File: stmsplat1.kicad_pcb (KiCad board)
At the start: 2 copper layers, 63 parts, among them CN1 Conn_01x16_Male, CN2 Conn_01x30_Male, CN3 Conn_01x20_Male, CN4 Conn_01x34_Male, CN5 10n, J1 Conn_Coaxial, J2 Conn_01x04_Male, U1 NUCLEO144-F746ZG, U10 MPL315A2, U11 XBee_SMT, U2 ublox_chinese_PCB_module, U3 HMC544A-RF_Switch, U4 Opamp_Quad_MCP6024, U5 AD8310, U6 MCP6S93-X_UN, U7 ADG729, U8 74HC04, U9 HMC544A-RF_Switch

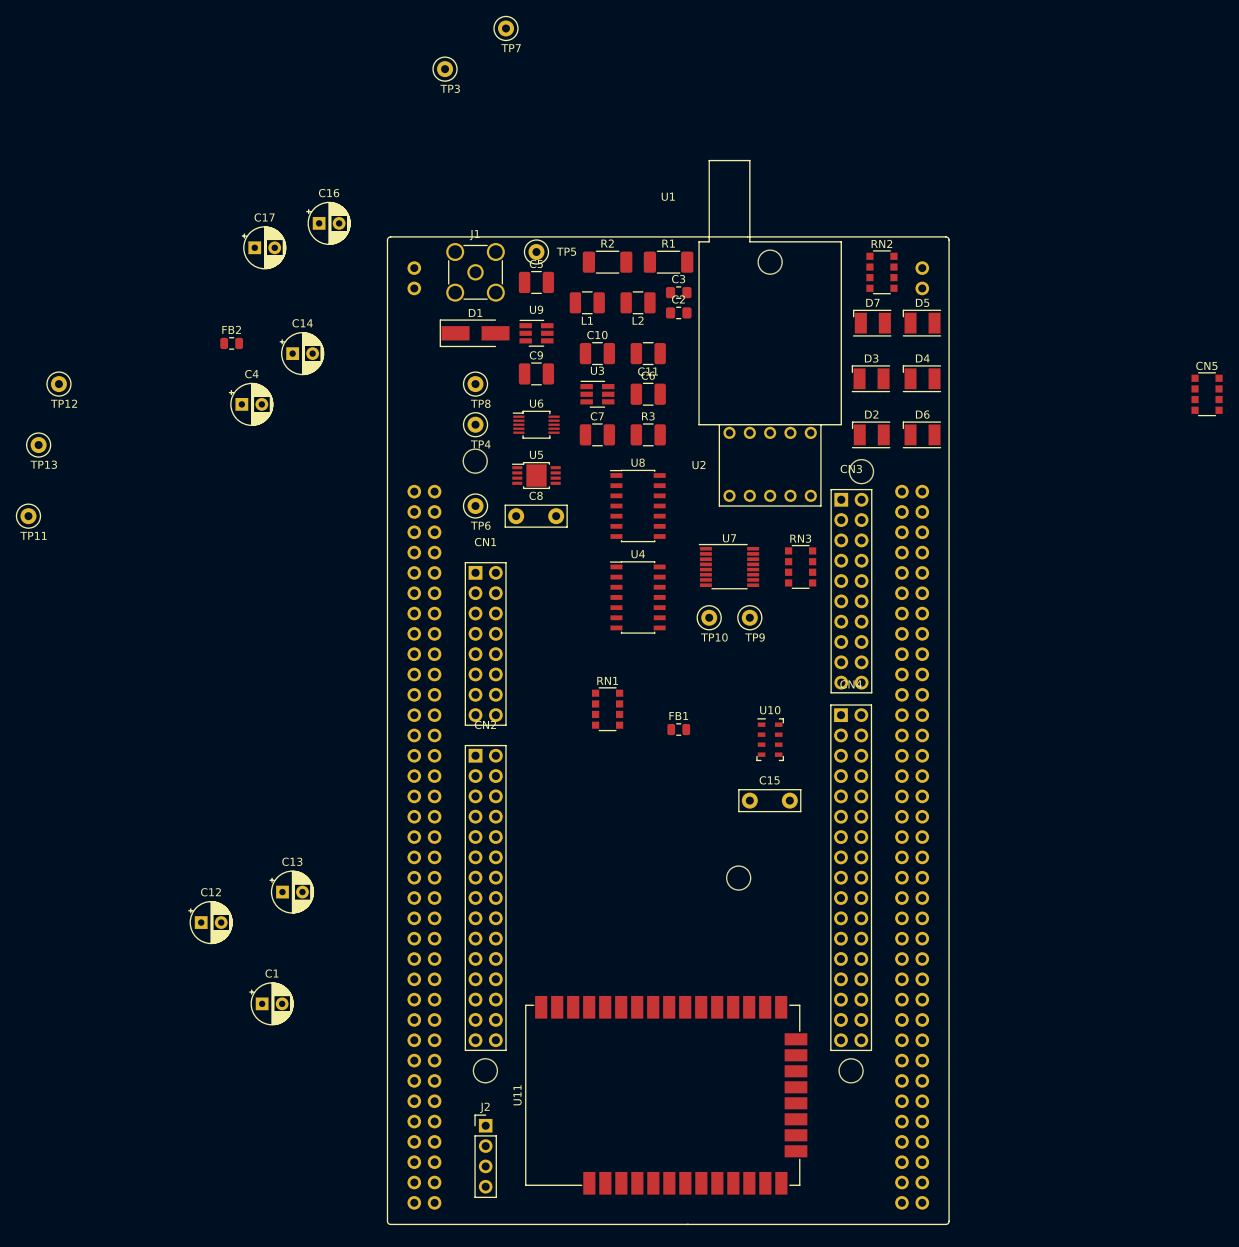
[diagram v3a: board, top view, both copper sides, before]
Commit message: XBee changes, more STM interconnect detail
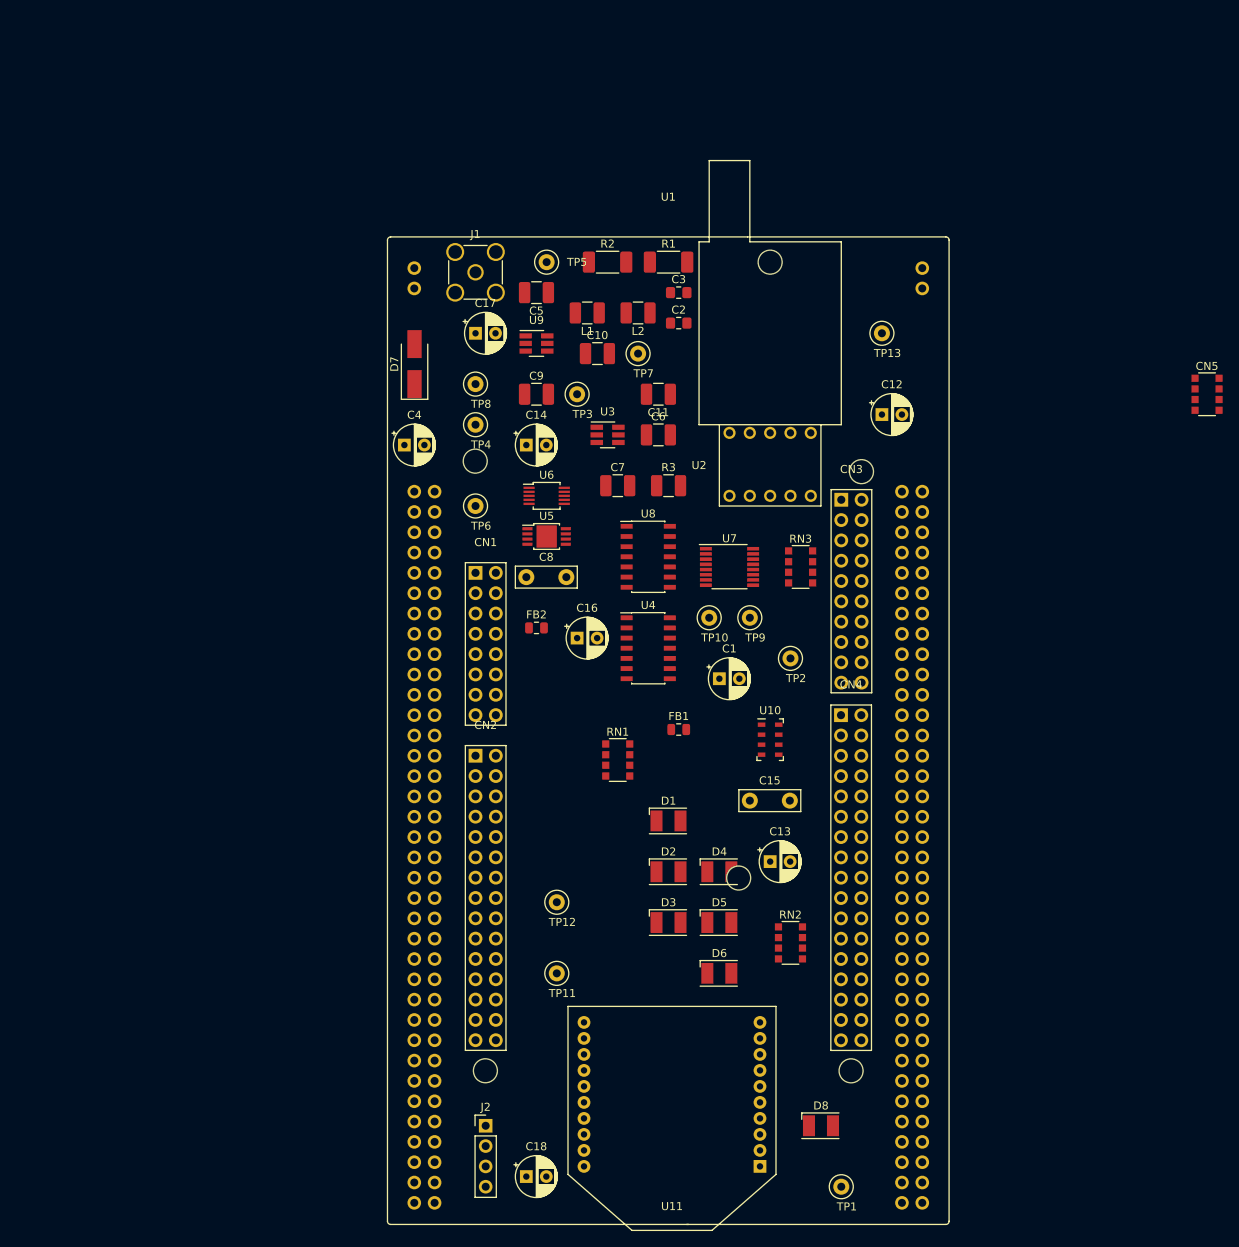
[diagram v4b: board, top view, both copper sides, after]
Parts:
- added C18: 10uF, Capacitor_THT:CP_Radial_D5.0mm_P2.50mm, F.Cu at (72.4, 151.1)
- added D8: LED, LED_SMD:LED_PLCC-2, F.Cu at (109.2, 144.8)
- added TP1: TestPoint, TestPoint:TestPoint_Loop_D1.80mm_Drill1.0mm_Beaded, F.Cu at (111.8, 152.4)
- added TP2: TestPoint, TestPoint:TestPoint_Loop_D1.80mm_Drill1.0mm_Beaded, F.Cu at (105.4, 86.4)
- D1: value SMAJ8.0CA Bourns 9V -> LED; footprint Diode_SMD:D_SMA_Handsoldering -> LED_SMD:LED_PLCC-2
- D7: value LED -> SMAJ8.0CA Bourns 9V; footprint LED_SMD:LED_PLCC-2 -> Diode_SMD:D_SMA_Handsoldering
- U11: value XBee_SMT -> XBee3; footprint RF_Module:Digi_XBee_SMT -> spatboard:XBEE-22MM-TH
- moved TP13 106.3 mm to (116.8, 45.7)
- moved C12 106.2 mm to (116.8, 55.9)
- moved TP12 89.8 mm to (76.2, 116.8)
- moved TP11 87.3 mm to (76.2, 125.7)
- moved RN2 84.6 mm to (105.4, 121.9)
- moved D5 79.1 mm to (96.5, 119.4)
- moved D3 72.6 mm to (90.2, 119.4)
- moved D6 71.9 mm to (96.5, 125.7)
- moved C1 70.1 mm to (96.5, 88.9)
- moved D4 66.7 mm to (96.5, 113.0)
- moved D1 65.6 mm to (90.2, 106.7)
- moved C13 61.1 mm to (102.9, 111.8)
- moved C16 61.0 mm to (78.7, 83.8)
- moved D2 60.2 mm to (90.2, 113.0)
- moved D7 57.5 mm to (58.4, 49.6), turned to 90 degrees
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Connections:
- D1 pad 1: Net-(C5-Pad1) -> GND
- D1 pad 2: AGND -> Net-(D1-Pad2)
- D7 pad 1: GND -> Net-(C5-Pad1)
- D7 pad 2: Net-(D7-Pad2) -> AGND
- FB2 pad 2: Net-(FB2-Pad2) -> GND
- J2 pad 2: /NXRX -> /PC12
- J2 pad 3: /NXTX -> /PB12
- RN2 pad 1: Net-(D4-Pad2) -> Net-(D1-Pad2)
- RN2 pad 2: Net-(D3-Pad2) -> Net-(D2-Pad2)
- RN2 pad 3: Net-(D2-Pad2) -> Net-(D4-Pad2)
- RN2 pad 4: Net-(D5-Pad2) -> Net-(D3-Pad2)
- RN2 pad 5: Net-(RN2-Pad5) -> /PD14
- RN2 pad 6: Net-(RN2-Pad6) -> /PD13
- RN2 pad 7: Net-(RN2-Pad7) -> /PD12
- RN2 pad 8: Net-(RN2-Pad8) -> /PD11
- RN3 pad 1: Net-(D7-Pad2) -> Net-(D5-Pad2)
- RN3 pad 2: Net-(RN3-Pad2) -> GND
- RN3 pad 7: Net-(RN3-Pad7) -> /XB_PIO4
- RN3 pad 8: Net-(RN3-Pad8) -> /PD15
- TP13 pad 1: Net-(TP13-Pad1) -> GND
- U11 pad 1: Net-(U11-Pad1) -> /+3V3
- U11 pad 10: Net-(U11-Pad10) -> GND
- U11 pad 12: Net-(U11-Pad12) -> /PA15
- U11 pad 16: Net-(U11-Pad16) -> /PB15
- U11 pad 19: Net-(U11-Pad19) -> Net-(TP12-Pad1)
- U11 pad 2: Net-(U11-Pad2) -> /PC11
- U11 pad 20: Net-(U11-Pad20) -> Net-(TP11-Pad1)
- U11 pad 3: Net-(U11-Pad3) -> /PA0
- U8 pad 1: Net-(U8-Pad1) -> /PE14

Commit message: Initial design captured
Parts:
- removed CN5: 10n, spatboard:C_Array_Convex_4x1206
- added C19: 1uF, Capacitor_THT:CP_Radial_D5.0mm_P2.50mm, F.Cu at (76.2, 95.2)
- added C20: 470pF, Capacitor_SMD:C_0805_2012Metric_Pad1.15x1.40mm_HandSolder, F.Cu at (74.3, 91.4)
- added LS1: Speaker, Buzzer_Beeper:MagneticBuzzer_Kingstate_KCG0601, F.Cu at (78.7, 109.2)
- added RN4: 4K7, Resistor_SMD:R_Array_Convex_4x1206, F.Cu at (119.4, 58.4)
- added U12: MIC5219-3.3YM5, Package_TO_SOT_SMD:SOT-23-5, F.Cu at (74.3, 88.2)
- moved TP7 41.3 mm to (78.7, 88.9)
- moved C12 5.68 mm to (119.4, 50.8)
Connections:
- net Net-(U7-Pad11) renamed /SPEAKER_TIM4CH3
- C1 pad 1: /+3V3 -> /P3V3
- C12 pad 1: /+3V3 -> /P3V3
- C13 pad 1: /+3V3 -> /P3V3
- C16 pad 1: /+3V3 -> /P3V3
- C18 pad 1: /+3V3 -> /P3V3
- FB1 pad 1: /+3V3 -> /P3V3
- RN2 pad 5: /PD14 -> /PD13
- RN2 pad 6: /PD13 -> /PD14
- RN3 pad 5: /+3V3 -> /P3V3
- TP3 pad 1: Net-(C9-Pad2) -> Net-(TP3-Pad1)
- TP7 pad 1: Net-(C10-Pad2) -> Net-(TP7-Pad1)
- TP9 pad 1: /DAC1 -> Net-(TP9-Pad1)
- U10 pad 1: /+3V3 -> /P3V3
- U10 pad 4: /+3V3 -> /P3V3
- U11 pad 1: /+3V3 -> /P3V3
- U11 pad 5: Net-(D8-Pad2) -> /PE15
- U11 pad 9: Net-(U11-Pad9) -> /PE10
- U2 pad 1: /+3V3 -> /P3V3
- U2 pad 5: Net-(U2-Pad5) -> /PB10
- U4 pad 1: Net-(U4-Pad1) -> Net-(TP3-Pad1)
- U4 pad 13: Net-(U4-Pad13) -> Net-(C19-Pad1)
- U4 pad 14: Net-(U4-Pad14) -> Net-(C19-Pad1)
- U4 pad 2: Net-(U4-Pad2) -> Net-(TP3-Pad1)
- U4 pad 3: Net-(U4-Pad3) -> /PA3
- U4 pad 5: Net-(U4-Pad5) -> Net-(U4-Pad12)
- U4 pad 6: Net-(U4-Pad6) -> Net-(TP9-Pad1)
- U4 pad 7: Net-(U4-Pad7) -> Net-(TP9-Pad1)
- U6 pad 6: Net-(U6-Pad6) -> /PG2
- U6 pad 7: Net-(U6-Pad7) -> /PC3
- U6 pad 8: Net-(U6-Pad8) -> /PC2
- U6 pad 9: Net-(U6-Pad9) -> /PD3
- U7 pad 10: Net-(U7-Pad10) -> /DAC1
- U7 pad 12: Net-(U7-Pad12) -> /LOGOUT
- U7 pad 8: Net-(U7-Pad8) -> /PA3
- U7 pad 9: Net-(U7-Pad9) -> Net-(U4-Pad12)
- U8 pad 14: /+3V3 -> /P3V3
- U8 pad 8: Net-(U8-Pad8) -> Net-(TP7-Pad1)
- U8 pad 9: Net-(U8-Pad9) -> Net-(U11-Pad7)

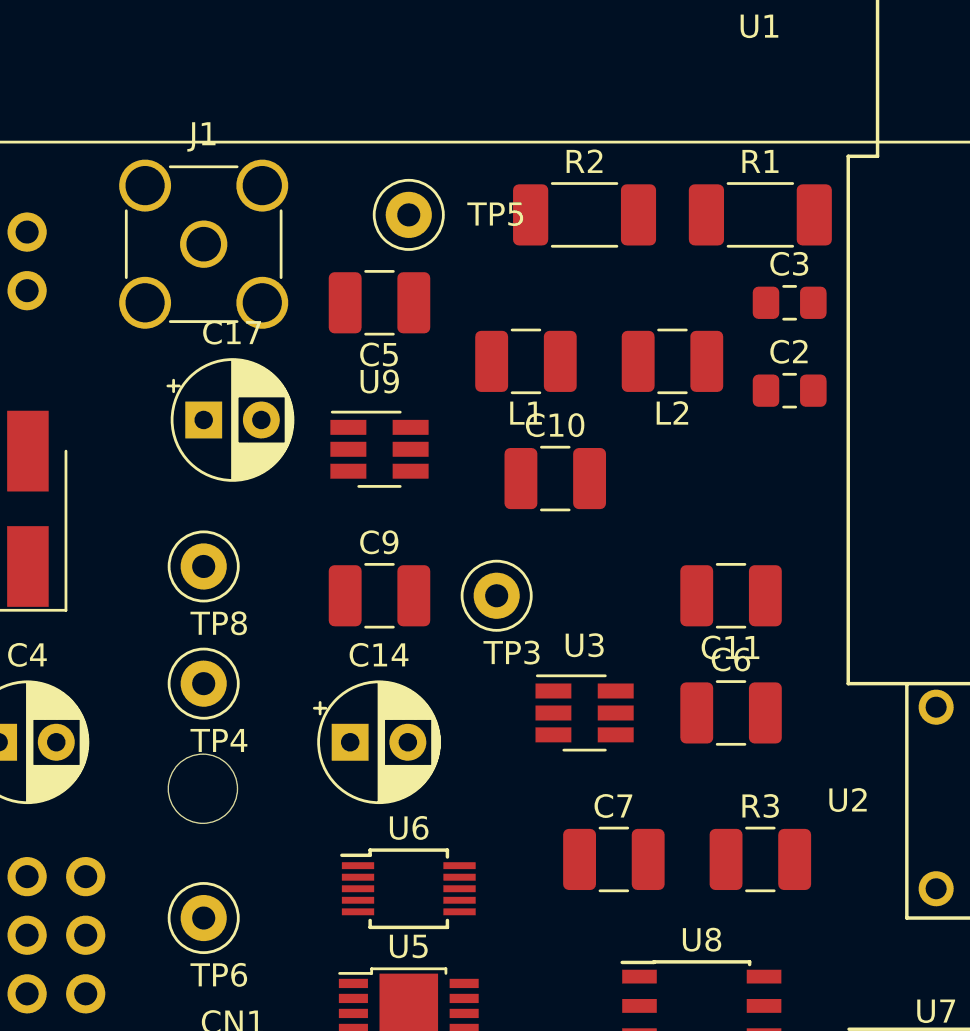
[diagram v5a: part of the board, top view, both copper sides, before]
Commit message: Chenged input and filter matching arrangement
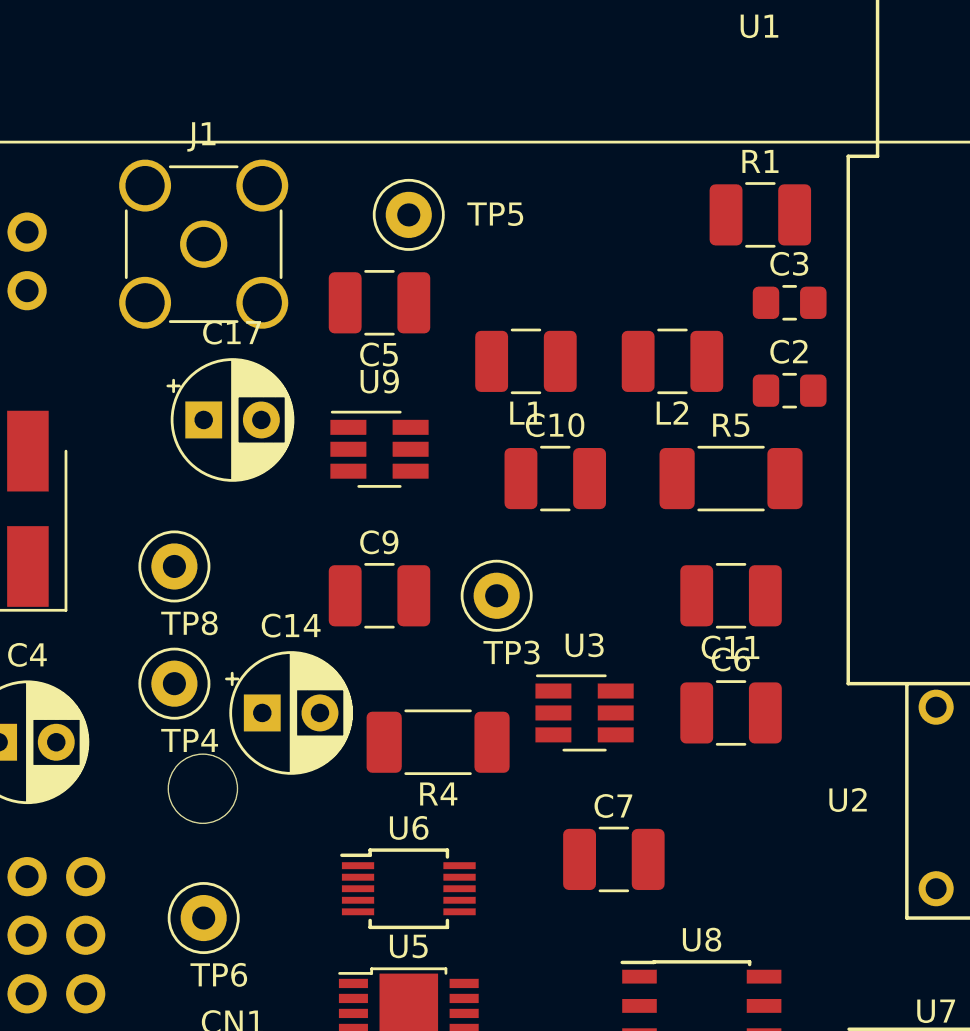
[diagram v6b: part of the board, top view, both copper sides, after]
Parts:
- removed R2: 100R, Resistor_SMD:R_2010_5025Metric_Pad1.52x2.65mm_HandSolder
- removed R3: 53R, Capacitor_SMD:C_1210_3225Metric_Pad1.42x2.65mm_HandSolder
- added R4: 100R, Resistor_SMD:R_2010_5025Metric_Pad1.52x2.65mm_HandSolder, F.Cu at (76.2, 59.7)
- added R5: 100R, Resistor_SMD:R_2010_5025Metric_Pad1.52x2.65mm_HandSolder, F.Cu at (88.9, 48.3)
- R1: value 100R -> 53R; footprint Resistor_SMD:R_2010_5025Metric_Pad1.52x2.65mm_HandSolder -> Capacitor_SMD:C_1210_3225Metric_Pad1.42x2.65mm_HandSolder
- moved C14 4.02 mm to (68.6, 58.4)
- moved TP4 1.27 mm to (64.8, 57.1)
- moved TP8 1.27 mm to (64.8, 52.1)
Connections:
- R1 pad 1: Net-(C10-Pad2) -> Net-(C5-Pad2)
- RN1 pad 2: Net-(C11-Pad1) -> Net-(RN1-Pad2)
- U11 pad 5: /PE15 -> Net-(D8-Pad2)

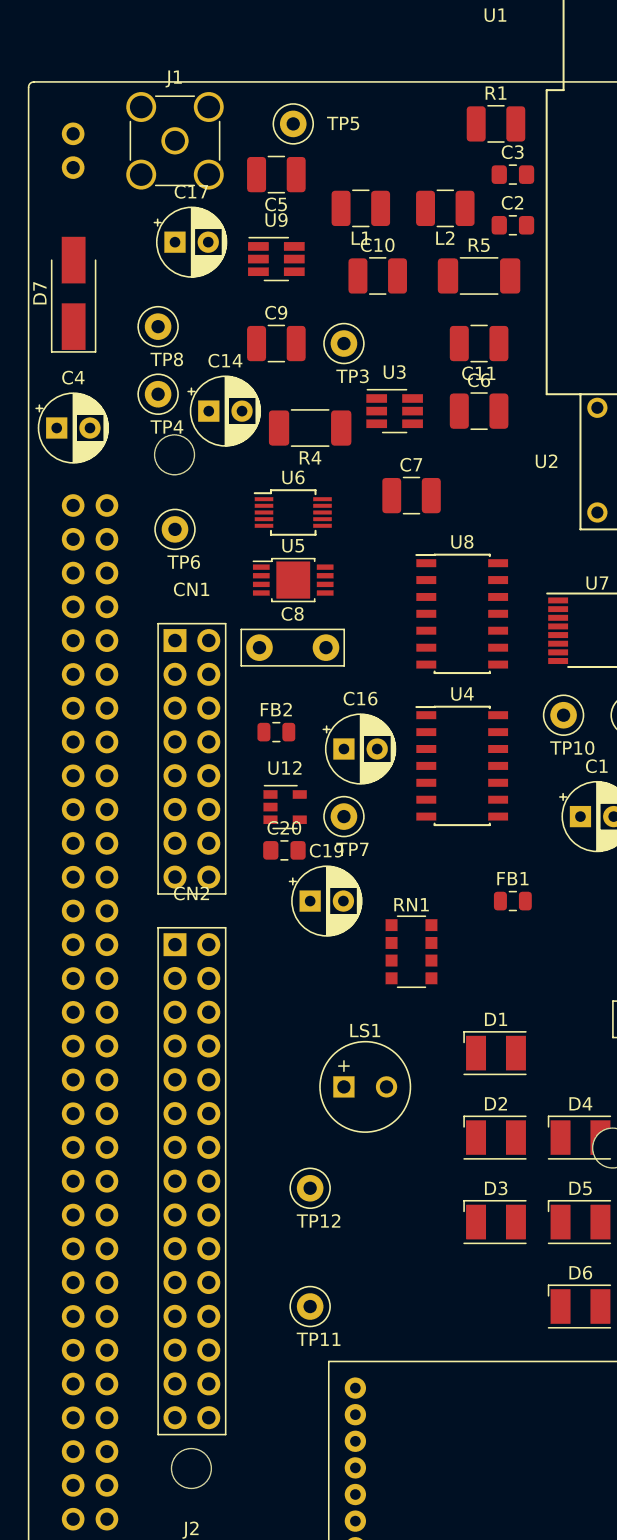
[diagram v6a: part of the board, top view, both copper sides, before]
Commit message: Add GPS and Debug Serial Comms connections
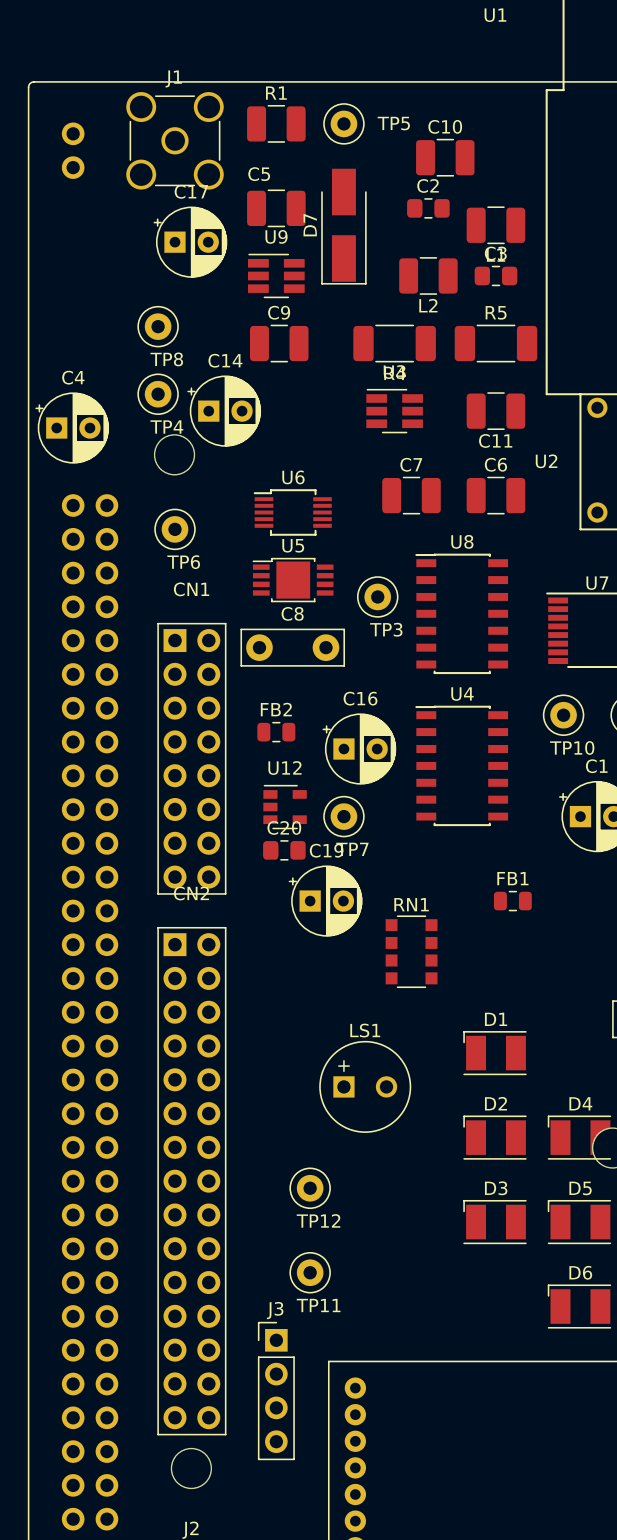
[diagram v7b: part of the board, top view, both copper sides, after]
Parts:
- added J3: Conn_01x04_Male, Connector_PinHeader_2.54mm:PinHeader_1x04_P2.54mm_Vertical, F.Cu at (73.7, 128.3)
- moved D7 21.0 mm to (78.7, 44.5)
- moved TP3 19.2 mm to (81.3, 72.4)
- moved R1 16.5 mm to (73.7, 36.8)
- moved C10 10.2 mm to (86.4, 39.4)
- moved L1 10.2 mm to (90.2, 44.5)
- moved R4 8.98 mm to (82.5, 53.3)
- moved C3 7.73 mm to (90.2, 48.3)
- moved C2 6.48 mm to (85.1, 43.2)
- moved C6 6.48 mm to (90.2, 64.8)
- moved R5 5.24 mm to (90.2, 53.3)
- moved C11 5.24 mm to (90.2, 58.4)
- moved L2 5.24 mm to (85.1, 48.3)
- moved TP5 3.81 mm to (78.7, 36.8)
- moved TP11 2.54 mm to (76.2, 123.2)
- moved C5 2.54 mm to (73.7, 43.2)
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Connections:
- U11 pad 5: Net-(D8-Pad2) -> /PE15
- U2 pad 3: Net-(U2-Pad3) -> /PG9
- U2 pad 4: Net-(U2-Pad4) -> /PC6

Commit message: placement improvements
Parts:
- U5: footprint Package_SO:MSOP-8-1EP_3x3mm_P0.65mm_EP2.54x2.8mm -> Package_SO:MSOP-8_3x3mm_P0.65mm
- moved TP2 57.1 mm to (59.7, 52.1)
- moved RN3 36.9 mm to (105.4, 111.8)
- moved C18 36.6 mm to (106.7, 138.4)
- moved C4 32.6 mm to (87.6, 71.1)
- moved FB1 26.9 mm to (82.5, 69.8)
- moved TP7 25.3 mm to (102.9, 81.3)
- moved C13 23.0 mm to (105.4, 88.9)
- moved TP10 20.4 mm to (96.5, 101.6)
- moved RN1 19.8 mm to (97.8, 85.1)
- moved U7 19.1 mm to (96.5, 94.0)
- moved C1 17.0 mm to (104.1, 73.7)
- moved C15 15.7 mm to (85.1, 100.3)
- moved U10 15.5 mm to (87.6, 94.0)
- moved D4 14.2 mm to (90.2, 125.7)
- moved TP4 8.98 mm to (66.0, 66.0)
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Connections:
- U8 pad 11: Net-(RN4-Pad2) -> Net-(RN4-Pad4)
- U8 pad 13: Net-(RN4-Pad4) -> Net-(RN4-Pad3)
- U8 pad 5: Net-(RN4-Pad3) -> Net-(RN4-Pad2)
